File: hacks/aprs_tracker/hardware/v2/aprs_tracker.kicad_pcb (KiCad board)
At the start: 2 copper layers, 39 parts, among them J1 3.5mm Stereo Jack, J2 2.5mm Stereo Jack, P1 POWER, P2 RADIO, P3 TEMPERATURE, P4 BAOFENG, P5 GPS, Q1 2N7002, Q2 2N7002, U1 arduino_mini

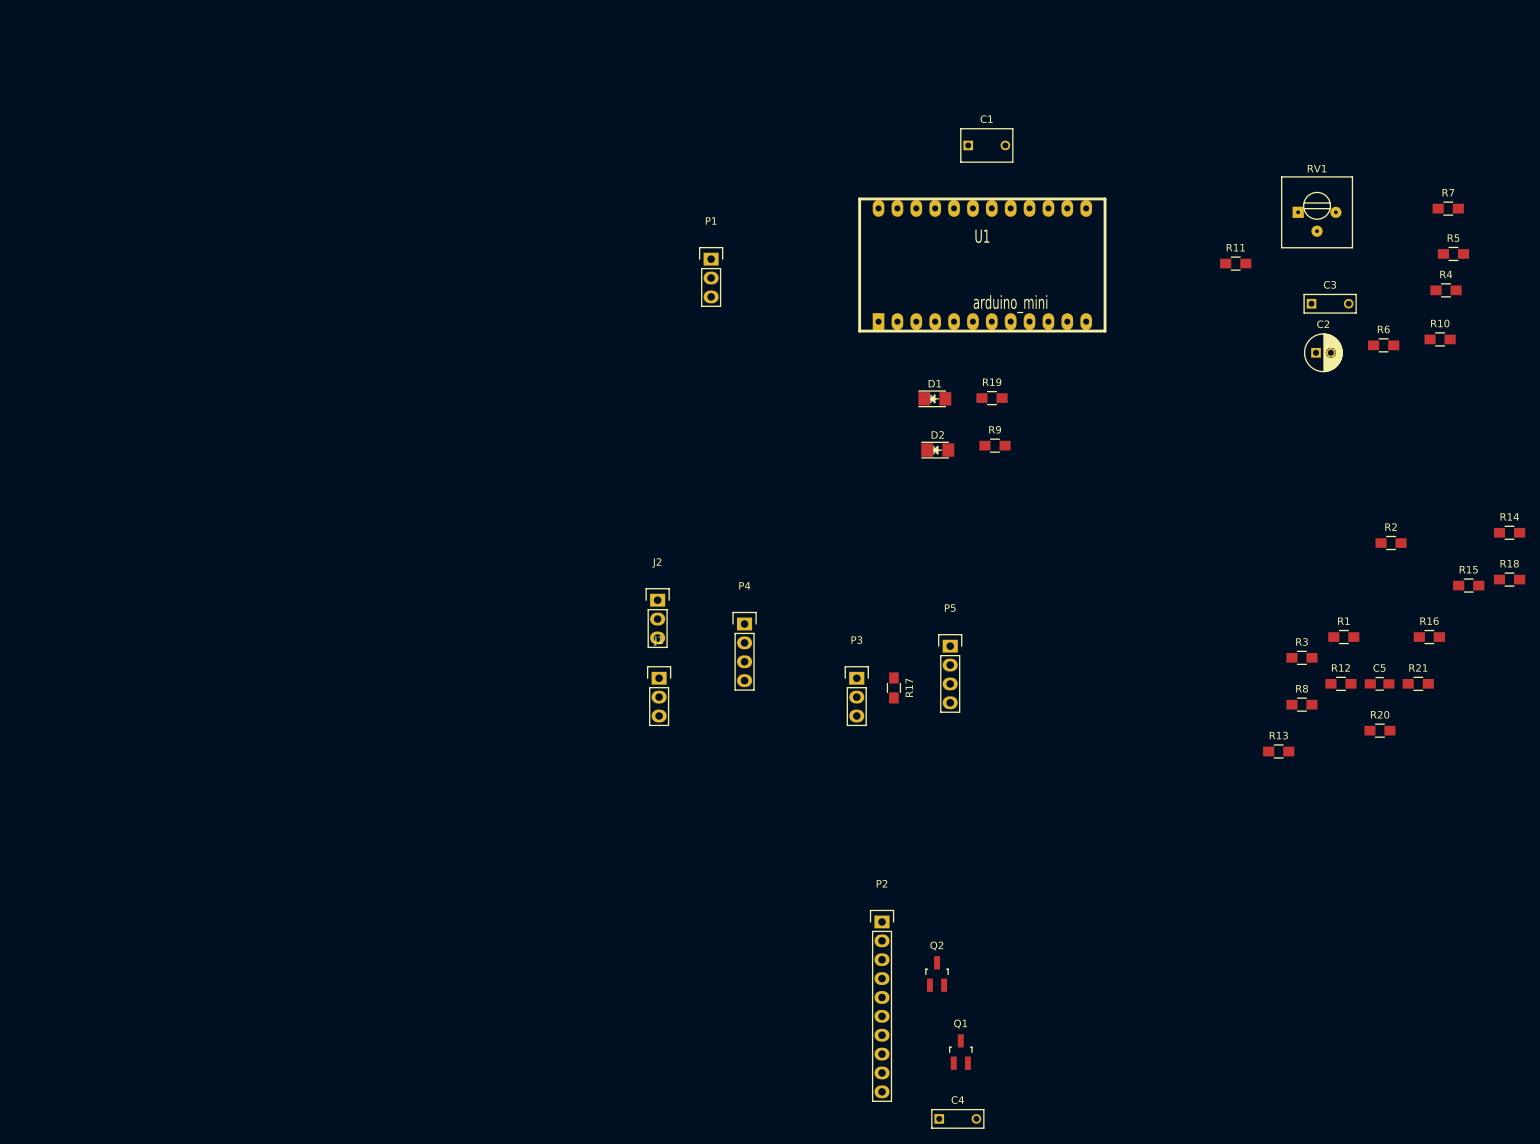
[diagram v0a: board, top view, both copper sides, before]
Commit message: started pcb placing
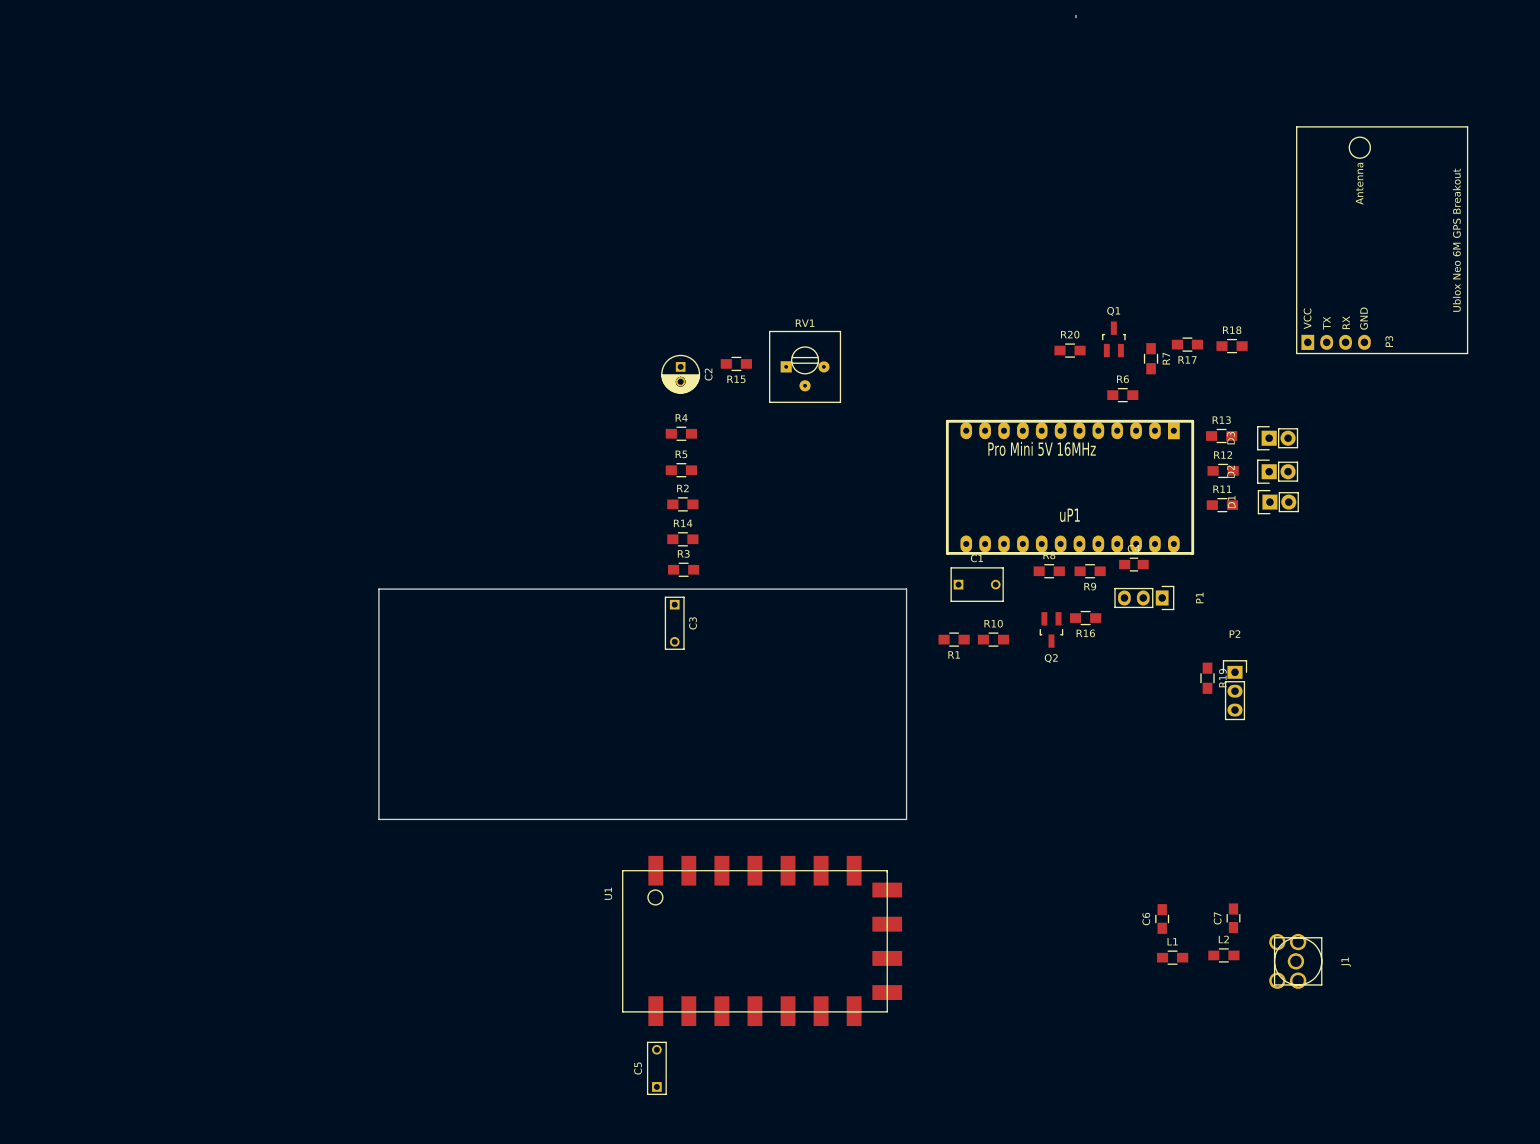
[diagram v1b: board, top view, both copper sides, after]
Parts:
- removed J2: 2.5mm Stereo Jack, Pin_Headers:Pin_Header_Straight_1x03
- removed P4: BAOFENG, Pin_Headers:Pin_Header_Straight_1x04
- removed P5: GPS, Pin_Headers:Pin_Header_Straight_1x04
- removed R21: 10K, Resistors_SMD:R_0805_HandSoldering
- added C6: 15pF, Capacitors_SMD:C_0805_HandSoldering, F.Cu at (196.8, 149.2)
- added C7: 15pF, Capacitors_SMD:C_0805_HandSoldering, F.Cu at (206.4, 149.1)
- added D3: STATUS (GREEN), Pin_Headers:Pin_Header_Straight_1x02, F.Cu at (211.2, 84.5)
- added L1: 0.027uH, Resistors_SMD:R_0805_HandSoldering, F.Cu at (198.2, 154.4)
- added L2: 0.027uH, Resistors_SMD:R_0805_HandSoldering, F.Cu at (205.1, 154.1)
- added uP1: Pro Mini 5V 16MHz, arduino pro mini:ARDUINO_PRO_MINI, F.Cu at (184.4, 87.3)
- C4: footprint Capacitors_ThroughHole:C_Rect_L7_W2.5_P5 -> Capacitors_SMD:C_0805_HandSoldering
- C5: footprint Capacitors_SMD:C_0805_HandSoldering -> Capacitors_ThroughHole:C_Rect_L7_W2.5_P5
- D1, D2: footprint LEDs:LED_1206 -> Pin_Headers:Pin_Header_Straight_1x02
- J1: value 3.5mm Stereo Jack -> SMA; footprint Pin_Headers:Pin_Header_Straight_1x03 -> sma_female_top:sma_female_top
- P2: value RADIO -> TEMPERATURE; footprint Pin_Headers:Pin_Header_Straight_1x10 -> Pin_Headers:Pin_Header_Straight_1x03
- P3: value TEMPERATURE -> GPS; footprint Pin_Headers:Pin_Header_Straight_1x03 -> ublox_gps:ublox_gps_breakout
- R1: value 1K -> 100K
- R10: value 270 1% -> 100K
- R11: value 100K -> 3K3
- R12: value 1K -> 3K3
- R13: value 10K -> 3K3
- R14: value 10K -> 270 1%
- R15: value 20K -> 100K
- R16: value 20K -> 10K
- R17: value 4.7K -> 10K
- R18: value 1K -> 20K
- R19: value 3K3 -> 4.7K
- R2: value 1K -> 1K 1%
- R3: value 100K -> 2K2 1%
- R4: value 1K 1% -> 3K9 1%
- R5: value 2K2 1% -> 8K2 1%
- R6: value 3K9 1% -> 1K
- R7: value 8K2 1% -> 1K
- R8: value 100K -> 1K
- R9: value 3K3 -> 1K
- U1: value arduino_mini -> DRA818V; footprint arduino pro mini:ARDUINO_PRO_MINI -> dra818v:dra818v
- moved C5 111.4 mm to (128.8, 171.8), turned to 90 degrees
- moved R14 111.2 mm to (132.3, 98.1)
- moved R5 107.9 mm to (132.1, 88.8)
- moved R4 104.7 mm to (132.1, 83.9)
- moved R15 103.0 mm to (139.5, 74.5), turned to 180 degrees
- moved Q1 98.1 mm to (190.3, 71.2)
- moved R2 95.4 mm to (132.3, 93.4)
- moved C3 94.8 mm to (131.2, 106.9), turned to 270 degrees
- moved J1 94.1 mm to (215.1, 154.9), turned to 90 degrees
- moved U1 91.5 mm to (124.2, 142.7)
- moved C2 85.5 mm to (132.0, 74.9), turned to 270 degrees
- moved R3 84.0 mm to (132.4, 102.2)
- moved C4 79.1 mm to (193.0, 101.5)
- moved P1 75.9 mm to (196.8, 106.0), turned to 270 degrees
- moved P3 75.7 mm to (216.4, 71.6), turned to 90 degrees
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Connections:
- C4 pad 1: Net-(C4-Pad1) -> +5V
- C4 pad 2: /MIC_LEVEL_OUT -> GND
- C5 pad 1: +5V -> /MIC_LEVEL_OUT
- C5 pad 2: GND -> Net-(C5-Pad2)
- J1 pad 1: (no net) -> Net-(C7-Pad1)
- J1 pad 2: (no net) -> GND
- J1 pad 3: (no net) -> GND
- P2 pad 1: Net-(P2-Pad1) -> +5V
- P2 pad 2: /LINE_LEVEL_IN -> /TEMP_DATA
- P2 pad 3: Net-(P2-Pad3) -> GND
- P3 pad 2: /TEMP_DATA -> /GPS_RX
- P3 pad 3: GND -> (no net)
- R1 pad 1: Net-(Q1-Pad2) -> /AUDIO_IN
- R1 pad 2: /PTT_CONTROL -> +5V
- R10 pad 1: Net-(C2-Pad2) -> /AUDIO_IN
- R11 pad 1: /MIC_LEVEL_OUT -> GND
- R11 pad 2: Net-(C2-Pad1) -> Net-(D1-Pad1)
- R12 pad 1: Net-(Q2-Pad2) -> GND
- R12 pad 2: /RADIO_PD_CONTROL -> Net-(D2-Pad1)
- R13 pad 1: Net-(P5-Pad2) -> GND
- R13 pad 2: /GPS_TX -> Net-(D3-Pad1)
- R14 pad 1: /RADIO_TX -> Net-(C2-Pad2)
- R14 pad 2: Net-(R14-Pad2) -> GND
- R15 pad 1: GND -> /MIC_LEVEL_OUT
- R15 pad 2: Net-(P5-Pad2) -> Net-(C2-Pad1)
- R16 pad 1: /RADIO_TX -> /V_BATT
- R16 pad 2: GND -> /RADIO_PD
- R17 pad 1: +5V -> /RADIO_TX
- R17 pad 2: /TEMP_DATA -> Net-(R17-Pad2)
- R18 pad 1: GND -> /RADIO_TX
- R18 pad 2: /RADIO_PD_CONTROL -> GND
- R19 pad 1: GND -> +5V
- R19 pad 2: Net-(D1-Pad1) -> /TEMP_DATA
- R2 pad 1: GND -> Net-(C2-Pad2)
- R2 pad 2: /PTT_CONTROL -> /D7
- R20 pad 1: Net-(P2-Pad3) -> Net-(R20-Pad1)
- R3 pad 1: /AUDIO_IN -> Net-(C2-Pad2)
- R3 pad 2: +5V -> /D6
- R4 pad 2: /D7 -> /D5
- R5 pad 2: /D6 -> /D4
- R6 pad 1: Net-(C2-Pad2) -> Net-(Q1-Pad2)
- R6 pad 2: /D5 -> /PTT_CONTROL
- R7 pad 1: Net-(C2-Pad2) -> GND
- R7 pad 2: /D4 -> /PTT_CONTROL
- R8 pad 1: /AUDIO_IN -> Net-(Q2-Pad2)
- R8 pad 2: GND -> /RADIO_PD_CONTROL
- R9 pad 2: Net-(D2-Pad1) -> /RADIO_PD_CONTROL
- U1 pad 1: Net-(U1-Pad1) -> (no net)
- U1 pad 10: Net-(U1-Pad10) -> GND
- U1 pad 11: Net-(U1-Pad11) -> (no net)
- U1 pad 12: +5V -> Net-(C6-Pad1)
- U1 pad 13: Net-(U1-Pad13) -> (no net)
- U1 pad 14: GND -> (no net)
- U1 pad 15: Net-(U1-Pad15) -> (no net)
- U1 pad 16: Net-(R14-Pad2) -> /RADIO_TX
- U1 pad 17: /GPS_RX -> (no net)
- U1 pad 18: Net-(U1-Pad18) -> Net-(C5-Pad2)
- U1 pad 2: Net-(U1-Pad2) -> (no net)
- U1 pad 3: Net-(U1-Pad3) -> /LINE_LEVEL_IN
- U1 pad 4: /AUDIO_IN -> (no net)
- U1 pad 5: /RADIO_PD_CONTROL -> Net-(R20-Pad1)
- U1 pad 6: /V_BATT -> /RADIO_PD
- U1 pad 7: Net-(U1-Pad7) -> (no net)
- U1 pad 8: Net-(U1-Pad8) -> /V_BATT
- U1 pad 9: Net-(U1-Pad9) -> GND
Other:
- board outline added: 93.8 x 108.2 mm

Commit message: initial placement ready
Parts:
- P3: moved to B.Cu
- moved J1 124.9 mm to (95.5, 119.0), turned to 0 degrees
- moved L2 120.1 mm to (95.1, 106.0), turned to 270 degrees
- moved P3 118.4 mm to (112.8, 128.9)
- moved C7 116.6 mm to (96.5, 110.2), turned to 0 degrees
- moved L1 116.4 mm to (95.1, 100.4), turned to 270 degrees
- moved C6 113.4 mm to (96.4, 96.4), turned to 0 degrees
- moved P1 107.2 mm to (93.3, 134.1), turned to 90 degrees
- moved R7 90.0 mm to (119.0, 121.5)
- moved Q1 89.6 mm to (115.2, 120.0)
- moved R6 87.4 mm to (117.6, 125.3)
- moved P2 86.3 mm to (121.7, 131.7), turned to 90 degrees
- moved R20 86.3 mm to (112.4, 120.2), turned to 270 degrees
- moved R19 80.8 mm to (123.0, 129.0), turned to 0 degrees
- moved C5 77.5 mm to (141.9, 95.4), turned to 180 degrees
- moved R9 73.6 mm to (118.0, 127.7), turned to 0 degrees
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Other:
- outline, holes or cut-outs redrawn

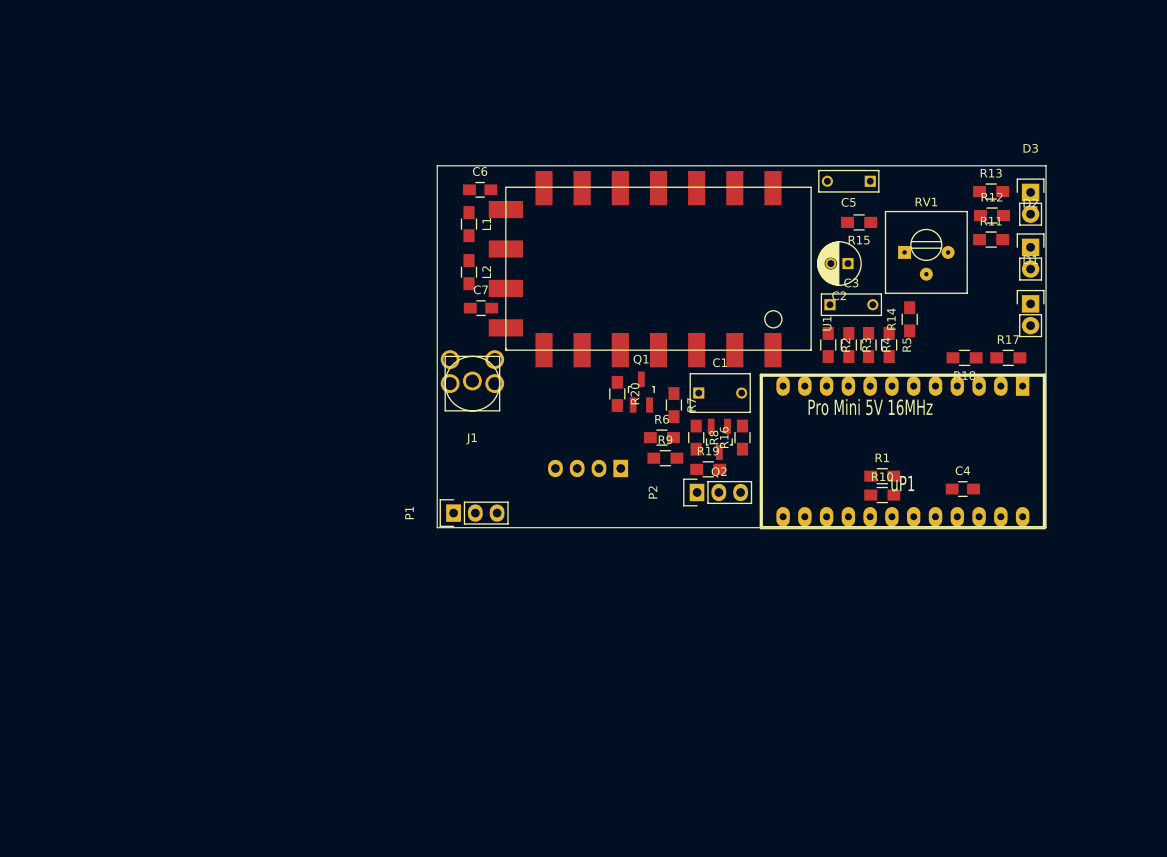
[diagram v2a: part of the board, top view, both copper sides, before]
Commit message: placed holes for box
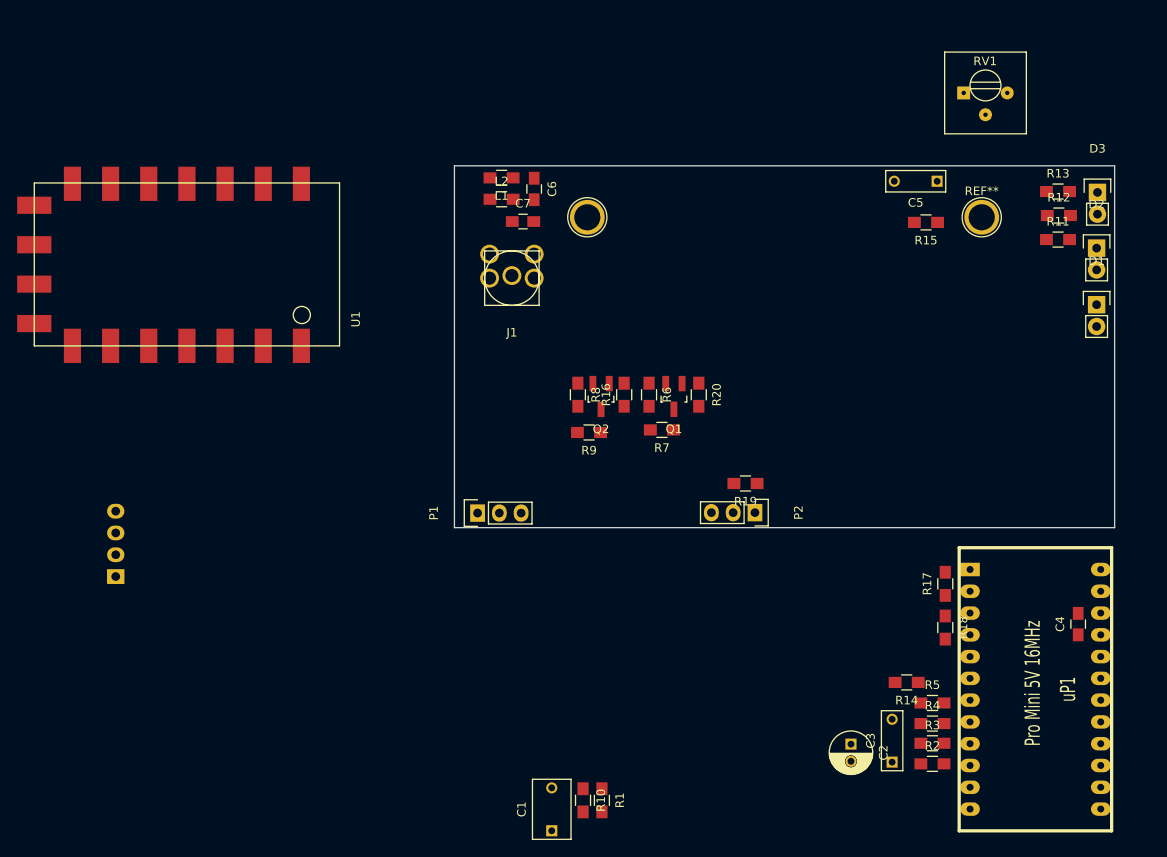
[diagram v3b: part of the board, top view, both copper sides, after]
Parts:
- added REF**: 1pin, Connect:1pin, F.Cu at (108.9, 99.6)
- added REF**: 1pin, Connect:1pin, F.Cu at (154.9, 99.6)
- moved P3 60.2 mm to (53.9, 141.5), turned to 0 degrees
- moved C2 56.1 mm to (139.7, 161.1), turned to 270 degrees
- moved U1 55.0 mm to (80.0, 114.6)
- moved C1 53.9 mm to (104.8, 171.2), turned to 90 degrees
- moved C3 53.8 mm to (144.4, 163.2), turned to 90 degrees
- moved R2 50.3 mm to (149.2, 163.3), turned to 0 degrees
- moved R1 50.0 mm to (110.6, 167.6), turned to 270 degrees
- moved R10 49.9 mm to (108.4, 167.6), turned to 270 degrees
- moved R3 47.5 mm to (149.2, 160.9), turned to 0 degrees
- moved R4 44.8 mm to (149.2, 158.7), turned to 0 degrees
- moved R14 42.4 mm to (146.2, 153.8), turned to 180 degrees
- moved R5 42.1 mm to (149.2, 156.2), turned to 0 degrees
- moved uP1 33.6 mm to (157.3, 154.7), turned to 270 degrees
- moved R18 31.5 mm to (150.7, 147.4), turned to 270 degrees
- moved R17 27.4 mm to (150.7, 142.3), turned to 90 degrees
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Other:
- board size 93.8 x 108.2 mm -> 91.8 x 108.2 mm

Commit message: placement with holes ready
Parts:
- moved R10 73.7 mm to (166.1, 121.7), turned to 90 degrees
- moved R1 69.9 mm to (163.4, 121.8), turned to 90 degrees
- moved U1 63.0 mm to (142.2, 124.7)
- moved C2 49.6 mm to (146.4, 111.9)
- moved C1 48.1 mm to (128.8, 129.5), turned to 0 degrees
- moved P3 44.1 mm to (96.1, 128.7)
- moved R18 36.3 mm to (156.5, 111.6)
- moved R17 36.1 mm to (156.5, 106.7)
- moved R14 35.7 mm to (149.1, 118.3), turned to 0 degrees
- moved C3 35.5 mm to (144.4, 127.7)
- moved R2 35.5 mm to (149.2, 127.8)
- moved R4 35.5 mm to (149.2, 123.2)
- moved R5 35.5 mm to (149.2, 120.8)
- moved R3 35.5 mm to (149.2, 125.5)
- moved uP1 35.4 mm to (157.6, 119.3)
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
